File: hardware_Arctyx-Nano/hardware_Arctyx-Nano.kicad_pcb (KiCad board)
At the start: 2 copper layers, 21 x 51 mm, 54 parts, among them J1 USB_C_Receptacle_USB2.0_16P, J2 Conn_01x20_Pin, J3 Conn_01x20_Pin, SW1 SW_Push, SW2 SW_Push, U1 ICE40UP5K-SG48ITR, U2 RP2350A-QFN60, U3 W25Q128JVS, U4 RT8075ZQW, U5 TJ-S1608SW6TDSLCCYRGB-A5, Y1 Crystal_GND24

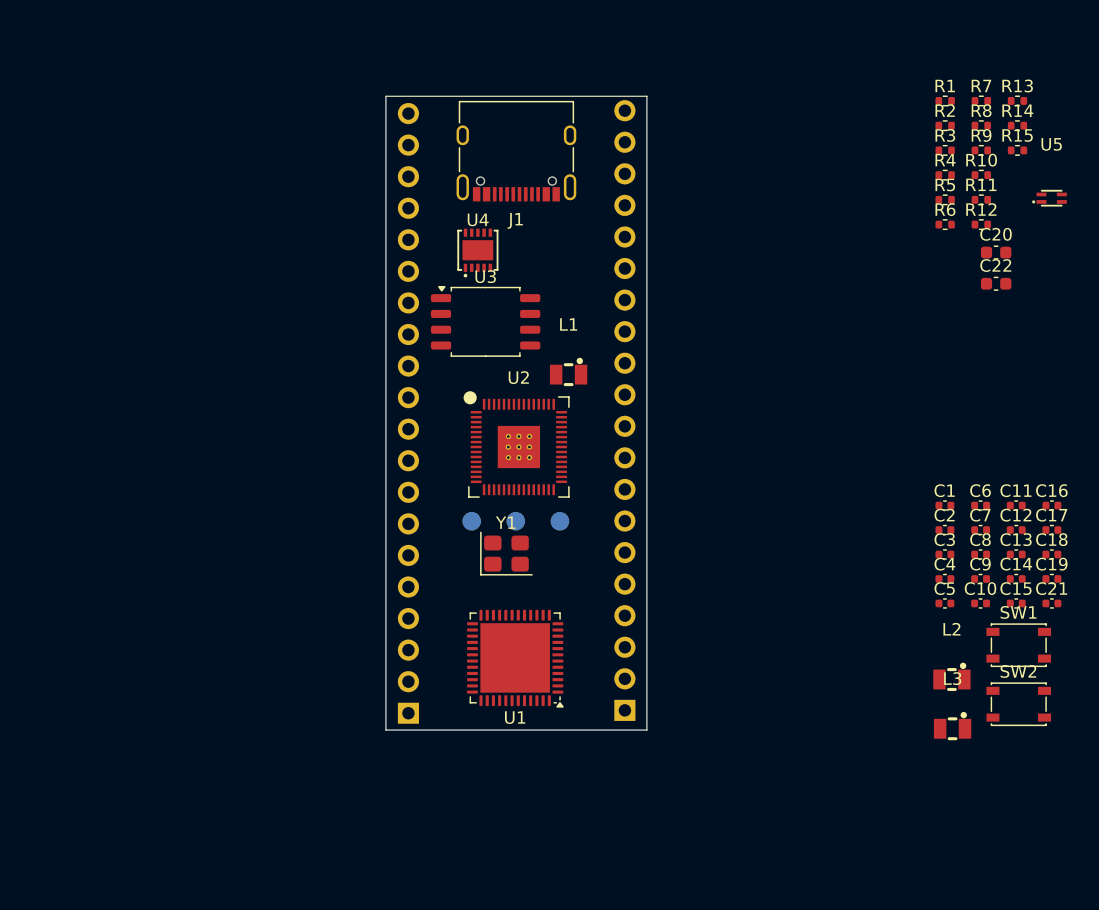
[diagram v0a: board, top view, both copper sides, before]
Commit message: Routing the PCB
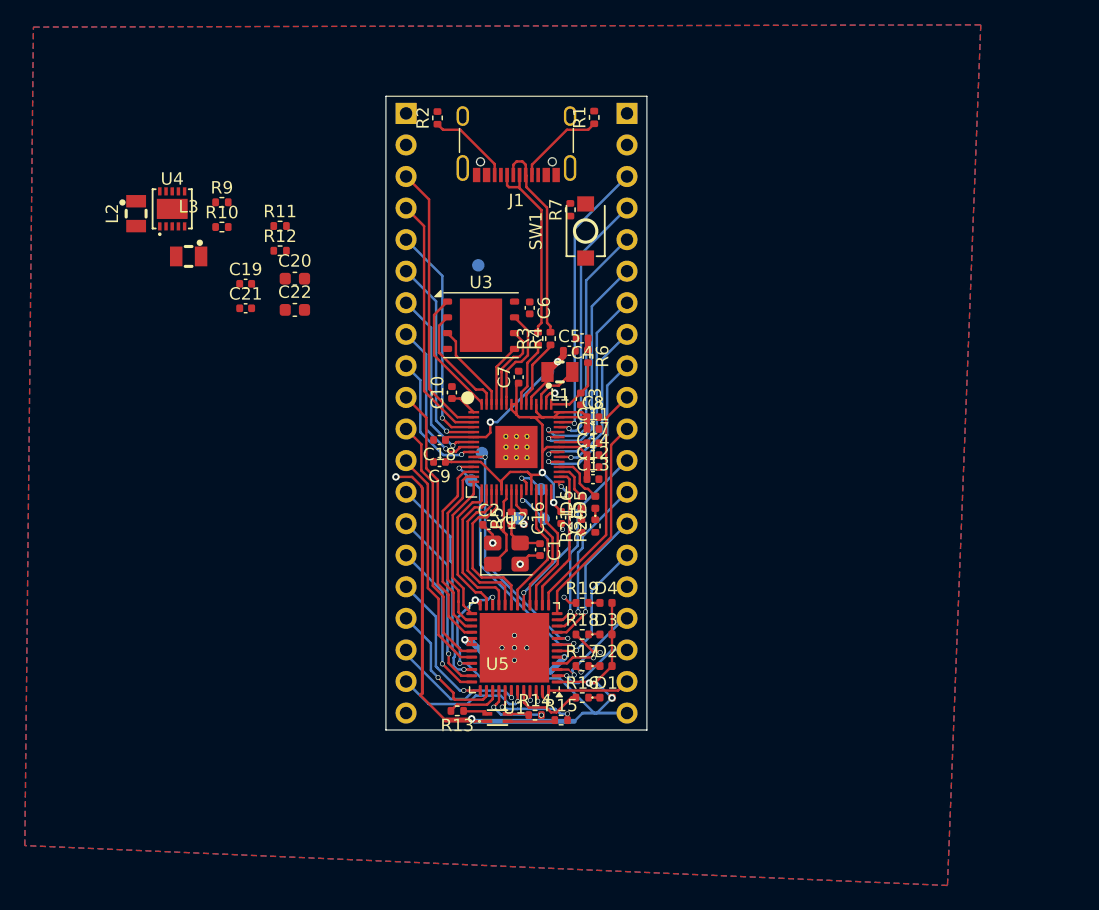
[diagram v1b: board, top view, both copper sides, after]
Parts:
- removed R8: 1k, Resistor_SMD:R_0402_1005Metric
- removed SW2: SW_Push, Button_Switch_SMD:SW_SPST_PTS810
- added D1: LED, LED_SMD:LED_0402_1005Metric, F.Cu at (167.7, 98.4)
- added D2: LED, LED_SMD:LED_0402_1005Metric, F.Cu at (167.7, 95.8)
- added D3: LED, LED_SMD:LED_0402_1005Metric, F.Cu at (167.7, 93.3)
- added D4: LED, LED_SMD:LED_0402_1005Metric, F.Cu at (167.7, 90.8)
- added D5: LED, LED_SMD:LED_0402_1005Metric, F.Cu at (166.8, 82.7)
- added D6: LED, LED_SMD:LED_0402_1005Metric, F.Cu at (165.7, 82.7)
- added R16: 100, Resistor_SMD:R_0402_1005Metric, F.Cu at (165.8, 98.4)
- added R17: 100, Resistor_SMD:R_0402_1005Metric, F.Cu at (165.8, 95.8)
- added R18: 100, Resistor_SMD:R_0402_1005Metric, F.Cu at (165.8, 93.3)
- added R19: 100, Resistor_SMD:R_0402_1005Metric, F.Cu at (165.8, 90.8)
- added R20: 100, Resistor_SMD:R_0402_1005Metric, F.Cu at (166.8, 84.6)
- added R21: 100, Resistor_SMD:R_0402_1005Metric, F.Cu at (165.7, 84.6)
- added TP4: TestPoint_Alt, TestPoint:TestPoint_Pad_D1.0mm, B.Cu at (163.0, 72.1)
- added TP5: TestPoint_Alt, TestPoint:TestPoint_Pad_D1.0mm, B.Cu at (156.9, 80.9)
- added TP6: TestPoint_Alt, TestPoint:TestPoint_Pad_D1.0mm, B.Cu at (157.7, 78.7)
- added TP7: TestPoint_Alt, TestPoint:TestPoint_Pad_D1.0mm, B.Cu at (157.4, 63.6)
- J2, J3: footprint Connector_PinSocket_2.54mm:PinSocket_1x20_P2.54mm_Vertical -> Connector_PinHeader_2.54mm:PinHeader_1x20_P2.54mm_Vertical
- L2, L3: value L -> AOTA-B201610S3R3-101-T
- SW1: footprint Button_Switch_SMD:SW_SPST_PTS810 -> easyeda2kicad:SW-SMD_L3.9-W3.0-P4.45
- TP1, TP2, TP3: footprint TestPoint:TestPoint_Pad_D1.5mm -> TestPoint:TestPoint_Pad_D1.0mm
- U3: value W25Q128JVS -> W25Q128JVP; footprint Package_SO:SOIC-8_5.3x5.3mm_P1.27mm -> Package_SON:WSON-8-1EP_6x5mm_P1.27mm_EP3.4x4.3mm
- moved L2 75.6 mm to (129.9, 59.4), turned to 90 degrees
- moved L3 72.3 mm to (134.1, 62.9)
- moved C19 69.1 mm to (138.7, 65.1)
- moved C21 69.1 mm to (138.7, 67.1)
- moved R13 66.6 mm to (155.7, 99.5), turned to 180 degrees
- moved R14 61.3 mm to (162.0, 99.8)
- moved R10 61.3 mm to (136.8, 60.5)
- moved R9 61.3 mm to (136.8, 58.5)
- moved U5 61.1 mm to (159.0, 100.0)
- moved R15 58.7 mm to (164.1, 100.2)
- moved C20 56.5 mm to (142.7, 64.7)
- moved C22 56.5 mm to (142.7, 67.2)
- moved R11 56.5 mm to (141.5, 60.4)
- moved R12 56.5 mm to (141.5, 62.4)
- moved C18 50.1 mm to (154.3, 77.7), turned to 180 degrees
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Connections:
- J2 pad 1: unconnected-(J2-Pin_1-Pad1) -> VBUS
- J2 pad 10: unconnected-(J2-Pin_10-Pad10) -> /IO1
- J2 pad 11: unconnected-(J2-Pin_11-Pad11) -> /IO2
- J2 pad 12: unconnected-(J2-Pin_12-Pad12) -> /IO3
- J2 pad 13: unconnected-(J2-Pin_13-Pad13) -> /IO4
- J2 pad 14: unconnected-(J2-Pin_14-Pad14) -> /IO5
- J2 pad 15: unconnected-(J2-Pin_15-Pad15) -> /IO6
- J2 pad 16: unconnected-(J2-Pin_16-Pad16) -> /IO7
- J2 pad 17: unconnected-(J2-Pin_17-Pad17) -> /IO8
- J2 pad 18: unconnected-(J2-Pin_18-Pad18) -> /IO9
- J2 pad 19: unconnected-(J2-Pin_19-Pad19) -> /IO10
- J2 pad 2: unconnected-(J2-Pin_2-Pad2) -> GND
- J2 pad 20: unconnected-(J2-Pin_20-Pad20) -> GND
- J2 pad 3: unconnected-(J2-Pin_3-Pad3) -> /GP0
- J2 pad 4: unconnected-(J2-Pin_4-Pad4) -> /GP1
- J2 pad 5: unconnected-(J2-Pin_5-Pad5) -> /GP2
- J2 pad 6: unconnected-(J2-Pin_6-Pad6) -> /GP3
- J2 pad 7: unconnected-(J2-Pin_7-Pad7) -> /GP4
- J2 pad 8: unconnected-(J2-Pin_8-Pad8) -> /GP5
- J2 pad 9: unconnected-(J2-Pin_9-Pad9) -> /GP6
- J3 pad 1: unconnected-(J3-Pin_1-Pad1) -> 3v3
- J3 pad 10: unconnected-(J3-Pin_10-Pad10) -> /IO20
- J3 pad 11: unconnected-(J3-Pin_11-Pad11) -> /IO19
- J3 pad 12: unconnected-(J3-Pin_12-Pad12) -> /IO18
- J3 pad 13: unconnected-(J3-Pin_13-Pad13) -> /IO17
- J3 pad 14: unconnected-(J3-Pin_14-Pad14) -> /IO16
- J3 pad 15: unconnected-(J3-Pin_15-Pad15) -> /IO15
- J3 pad 16: unconnected-(J3-Pin_16-Pad16) -> /IO14
- J3 pad 17: unconnected-(J3-Pin_17-Pad17) -> /IO13
- J3 pad 18: unconnected-(J3-Pin_18-Pad18) -> /IO12
- J3 pad 19: unconnected-(J3-Pin_19-Pad19) -> /IO11
- J3 pad 2: unconnected-(J3-Pin_2-Pad2) -> GND
- J3 pad 20: unconnected-(J3-Pin_20-Pad20) -> 3v3
- J3 pad 3: unconnected-(J3-Pin_3-Pad3) -> /GP29
- J3 pad 4: unconnected-(J3-Pin_4-Pad4) -> /GP28
- J3 pad 5: unconnected-(J3-Pin_5-Pad5) -> /GP27
- J3 pad 6: unconnected-(J3-Pin_6-Pad6) -> /GP26
- J3 pad 7: unconnected-(J3-Pin_7-Pad7) -> /GP25
- J3 pad 8: unconnected-(J3-Pin_8-Pad8) -> /GP24
- J3 pad 9: unconnected-(J3-Pin_9-Pad9) -> /GP23
- L2 pad 1: Net-(U4-LX1) -> 1v2
- L2 pad 2: 1v2 -> Net-(U4-LX1)
- L3 pad 1: 3v3 -> Net-(U4-LX2)
- L3 pad 2: Net-(U4-LX2) -> 3v3
- U1 pad 10: unconnected-(U1B-IOB_18a-Pad10) -> /IO17
- U1 pad 11: unconnected-(U1B-IOB_20a-Pad11) -> /IO18
- U1 pad 12: unconnected-(U1B-IOB_22a-Pad12) -> /IO19
- U1 pad 13: unconnected-(U1B-IOB_24a-Pad13) -> /IO20
- U1 pad 18: unconnected-(U1B-IOB_31b-Pad18) -> /BUS7
- U1 pad 19: unconnected-(U1B-IOB_29b-Pad19) -> /BUS6
- U1 pad 2: unconnected-(U1C-IOB_6a-Pad2) -> /IO12
- U1 pad 20: unconnected-(U1B-IOB_25b_G3-Pad20) -> /BUS5
- U1 pad 21: unconnected-(U1B-IOB_23b-Pad21) -> /BUS4
- U1 pad 23: unconnected-(U1A-IOT_37a-Pad23) -> /BUS3
- U1 pad 25: unconnected-(U1A-IOT_36b-Pad25) -> /BUS2
- U1 pad 26: unconnected-(U1A-IOT_39a-Pad26) -> /BUS1
- U1 pad 27: unconnected-(U1A-IOT_38b-Pad27) -> /BUS0
- U1 pad 28: unconnected-(U1A-IOT_41a-Pad28) -> /IO1
- U1 pad 3: unconnected-(U1C-IOB_9b-Pad3) -> /IO13
- U1 pad 31: unconnected-(U1A-IOT_42b-Pad31) -> /IO2
- U1 pad 32: unconnected-(U1A-IOT_43a-Pad32) -> /IO3
- U1 pad 34: unconnected-(U1A-IOT_44b-Pad34) -> /IO4
- U1 pad 35: unconnected-(U1A-IOT_46b_G0-Pad35) -> /IO5
- U1 pad 36: unconnected-(U1A-IOT_48b-Pad36) -> /IO6
- U1 pad 37: unconnected-(U1A-IOT_45a_G1-Pad37) -> /IO7
- U1 pad 38: unconnected-(U1A-IOT_50b-Pad38) -> /IO8
- U1 pad 4: unconnected-(U1C-IOB_8a-Pad4) -> /IO14
- U1 pad 42: unconnected-(U1A-IOT_51a-Pad42) -> /IO9
- U1 pad 43: unconnected-(U1A-IOT_49a-Pad43) -> /IO10
- U1 pad 44: unconnected-(U1C-IOB_3b_G6-Pad44) -> Net-(U1C-IOB_3b_G6)
- U1 pad 45: unconnected-(U1C-IOB_5b-Pad45) -> Net-(U1C-IOB_5b)
- U1 pad 46: unconnected-(U1C-IOB_0a-Pad46) -> Net-(U1C-IOB_0a)
- U1 pad 47: unconnected-(U1C-IOB_2a-Pad47) -> Net-(U1C-IOB_2a)
- U1 pad 48: unconnected-(U1C-IOB_4a-Pad48) -> /IO11
- U1 pad 6: unconnected-(U1B-IOB_13b-Pad6) -> /IO15
- U1 pad 9: unconnected-(U1B-IOB_16a-Pad9) -> /IO16
- U2 pad 10: unconnected-(U2-GPIO7-Pad10) -> CRESETN
- U2 pad 12: unconnected-(U2-GPIO8-Pad12) -> CDONE
- U2 pad 13: unconnected-(U2-GPIO9-Pad13) -> /BUS0
- U2 pad 14: unconnected-(U2-GPIO10-Pad14) -> /BUS1
- U2 pad 15: unconnected-(U2-GPIO11-Pad15) -> /BUS2
- U2 pad 16: unconnected-(U2-GPIO12-Pad16) -> /BUS3
- U2 pad 17: unconnected-(U2-GPIO13-Pad17) -> /BUS4
- U2 pad 18: unconnected-(U2-GPIO14-Pad18) -> /BUS5
- U2 pad 19: unconnected-(U2-GPIO15-Pad19) -> /BUS6
- U2 pad 2: unconnected-(U2-GPIO0-Pad2) -> /GP0
- U2 pad 26: Net-(U2-RUN) -> 3v3
- U2 pad 27: unconnected-(U2-GPIO16-Pad27) -> /BUS7
- U2 pad 3: unconnected-(U2-GPIO1-Pad3) -> /GP1
- U2 pad 33: unconnected-(U2-GPIO21-Pad33) -> Net-(D6-A)
- U2 pad 34: unconnected-(U2-GPIO22-Pad34) -> Net-(D5-A)
- U2 pad 35: unconnected-(U2-GPIO23-Pad35) -> /GP23
- U2 pad 36: unconnected-(U2-GPIO24-Pad36) -> /GP24
- U2 pad 37: unconnected-(U2-GPIO25-Pad37) -> /GP25
- U2 pad 4: unconnected-(U2-GPIO2-Pad4) -> /GP2
- U2 pad 40: unconnected-(U2-GPIO26_ADC0-Pad40) -> /GP26
- U2 pad 41: unconnected-(U2-GPIO27_ADC1-Pad41) -> /GP27
- U2 pad 42: unconnected-(U2-GPIO28_ADC2-Pad42) -> /GP28
- U2 pad 43: unconnected-(U2-GPIO29_ADC3-Pad43) -> /GP29
- U2 pad 5: unconnected-(U2-GPIO3-Pad5) -> /GP3
- U2 pad 7: unconnected-(U2-GPIO4-Pad7) -> /GP4
- U2 pad 8: unconnected-(U2-GPIO5-Pad8) -> /GP5
- U2 pad 9: unconnected-(U2-GPIO6-Pad9) -> /GP6
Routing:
- net 3v3: track 0.00 -> 125.0 mm, vias 0 -> 9
- net /GP29: track 0.00 -> 22.9 mm, vias 0 -> 1
- net /GP0: track 0.00 -> 22.4 mm
- net 1v1: track 0.00 -> 21.9 mm, vias 0 -> 2
- net /IO1: track 0.00 -> 21.4 mm
- net CDONE: track 0.00 -> 21.3 mm, vias 0 -> 2
- net /GP28: track 0.00 -> 21.2 mm, vias 0 -> 1
- net /GP27: track 0.00 -> 21.0 mm, vias 0 -> 1
- net /IO2: track 0.00 -> 20.5 mm
- net /GP1: track 0.00 -> 20.4 mm
- net CRESETN: track 0.00 -> 20.0 mm, vias 0 -> 2
- net /IO20: track 0.00 -> 19.3 mm
- net /GP26: track 0.00 -> 18.7 mm, vias 0 -> 1
- net /IO3: track 0.00 -> 18.5 mm
- net /GP2: track 0.00 -> 18.4 mm, vias 0 -> 1
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- added copper zone on B.Cu, net GND
- added copper zone on F.Cu, net GND

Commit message: PCB Routing
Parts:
- added C23: 4.7u, Capacitor_SMD:C_0402_1005Metric, F.Cu at (154.9, 92.6)
- moved L3 27.1 mm to (161.2, 61.6), turned to 90 degrees
- moved U4 25.4 mm to (158.1, 61.7)
- moved L2 25.2 mm to (154.9, 61.7)
- moved C21 23.6 mm to (160.9, 59.1)
- moved R10 22.9 mm to (159.4, 64.5), turned to 180 degrees
- moved C20 22.9 mm to (165.5, 66.2), turned to 90 degrees
- moved R9 20.8 mm to (156.7, 64.5), turned to 180 degrees
- moved R12 17.7 mm to (158.8, 58.8)
- moved C19 16.2 mm to (154.9, 64.6), turned to -90 degrees
- moved R11 15.2 mm to (156.6, 58.9)
- moved C22 14.7 mm to (154.4, 58.4), turned to -90 degrees
- moved TP7 3.10 mm to (155.0, 61.7)
- moved R7 2.85 mm to (166.8, 57.1), turned to -90 degrees
- moved SW1 0.76 mm to (165.5, 61.4)
- moved J1 0.28 mm to (160.5, 52.4)
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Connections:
- R16 pad 1: Net-(U1C-IOB_3b_G6) -> Net-(U1C-IOB_2a)
- R17 pad 1: Net-(U1C-IOB_5b) -> Net-(U1C-IOB_0a)
- R18 pad 1: Net-(U1C-IOB_0a) -> Net-(U1C-IOB_5b)
- R19 pad 1: Net-(U1C-IOB_2a) -> Net-(U1C-IOB_3b_G6)
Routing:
- net 3v3: track 125.0 -> 61.5 mm, vias 9 -> 21
- net 1v2: track 12.0 -> 59.9 mm, vias 2 -> 5
- net GND: track 5.61 -> 27.1 mm, vias 10 -> 31
- net Q_SS: track 10.3 -> 29.8 mm, vias 0 -> 2
- net VBUS: track 0.00 -> 11.8 mm, vias 0 -> 6
- net 1v1: track 21.9 -> 33.0 mm, vias 2 -> 3
- net Net-(U1C-IOB_5b): track 1.45 -> 9.83 mm
- net Net-(U4-LX1): track 0.00 -> 7.77 mm
- net Net-(U4-LX2): track 0.00 -> 7.21 mm
- net /IO14: track 3.13 -> 10.1 mm
- net Net-(U1C-IOB_3b_G6): track 5.98 -> 11.2 mm, vias 0 -> 2
- net Net-(U4-FB1): track 0.00 -> 3.26 mm
- net Net-(U1C-IOB_0a): track 3.47 -> 6.38 mm
- net Net-(U4-FB2): track 0.00 -> 2.84 mm
- net Net-(R7-Pad2): track 0.00 -> 2.54 mm
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- added copper zone on In2.Cu, net 3v3
- added copper zone on In1.Cu, net GND
- added copper zone on In1.Cu, net VBUS
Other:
- copper layers 2 -> 4

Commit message: Fixing Silkscreen
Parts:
- added ?: , , F.Cu at (161.2, 78.9)
- added ?: , , F.Cu at (161.2, 77.5)
- added ?: , , F.Cu at (159.8, 78.9)
- added ?: , , F.Cu at (159.8, 77.5)
- moved TP3 4.66 mm to (158.3, 83.6)
- moved TP5 0.80 mm to (156.1, 81.0)
- moved TP6 0.70 mm to (157.7, 78.0)
- moved TP1 0.46 mm to (162.5, 83.6)
- moved TP2 0.41 mm to (160.4, 83.6)
- moved C20 0.40 mm to (165.5, 66.6)
- moved R14 0.22 mm to (161.8, 99.7)
- moved R13 0.15 mm to (155.7, 99.6)
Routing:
- net Net-(U2-SWDIO): track 3.01 -> 4.90 mm
- net D-: track 17.0 -> 18.8 mm
- net Net-(U1A-RGB1): track 5.85 -> 6.94 mm
- net GND: track 27.1 -> 26.1 mm, vias 31 -> 40
- net CRESETN: track 20.0 -> 20.9 mm
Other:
- board text added: "D1"
- board text added: "D2"
- board text added: "D3"
- board text added: "D4"
